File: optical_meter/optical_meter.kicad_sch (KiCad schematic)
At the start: 43 parts, among them J1 SFP+, J2 SFP+, J3 Conn_01x02_Pin, U2 FIN1002M5X, U3 FIN1001M5X

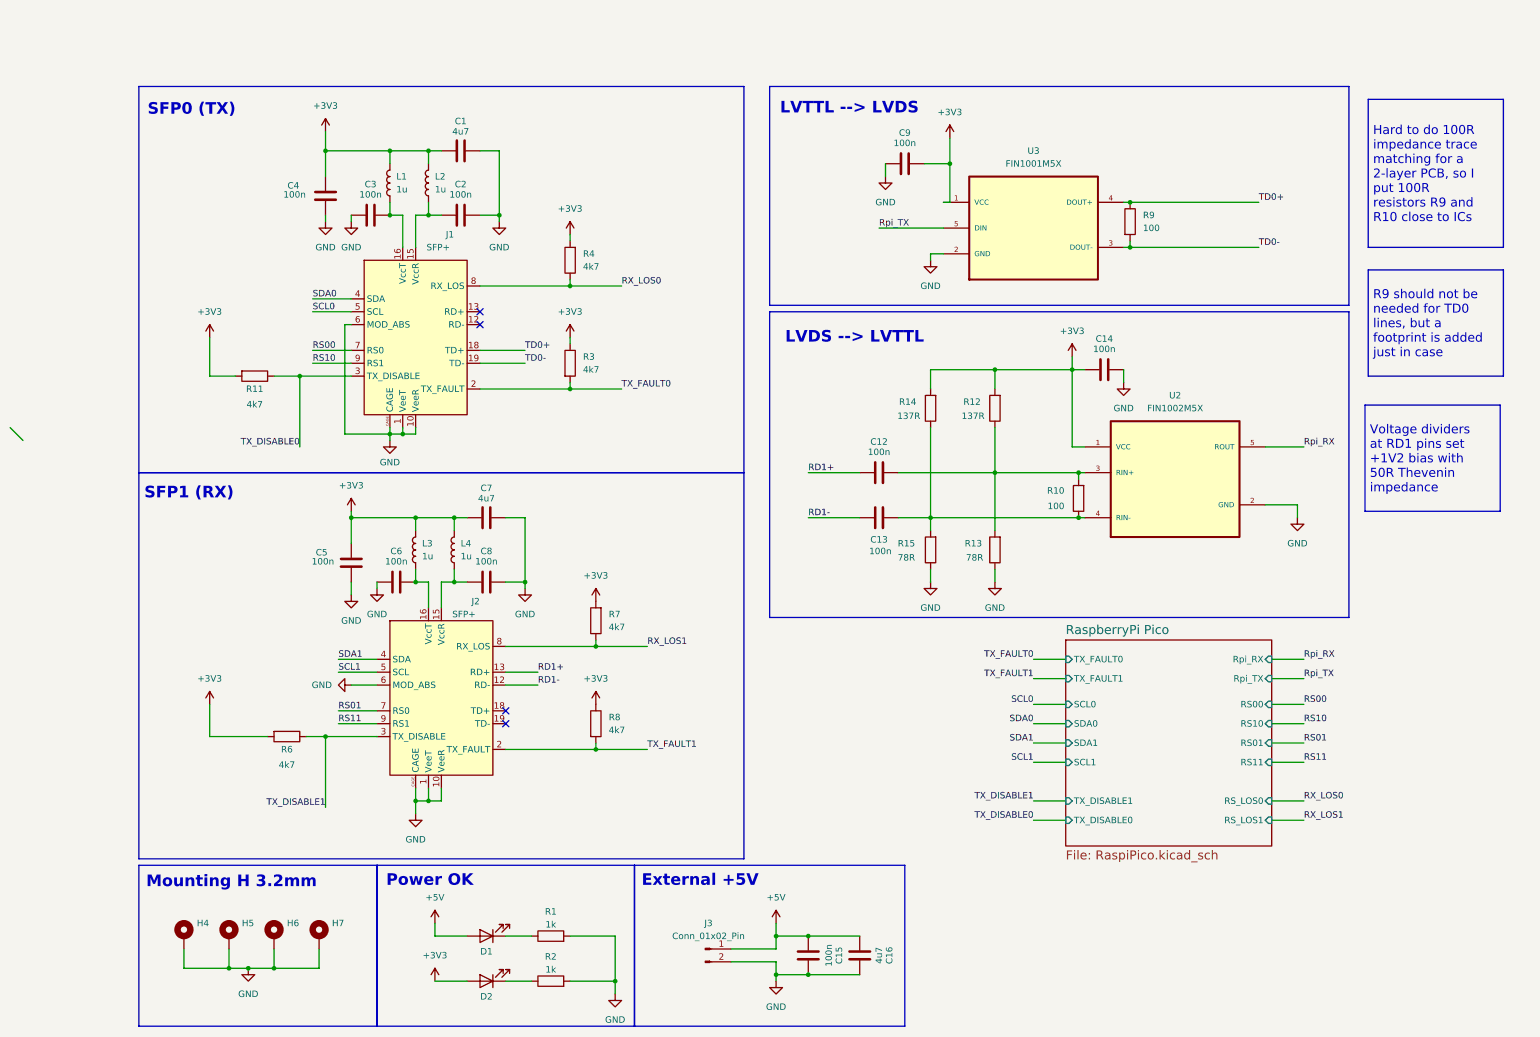
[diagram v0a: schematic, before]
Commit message: Removing one SFP connector - now the PCB will only work with full-duplex SFP/SFT+ connectors. Also did a major schematic cleanup: no hierarchal design, added 2 more GPIOs, DNP voltage dividers on LVDS lines creating +1V2 offset
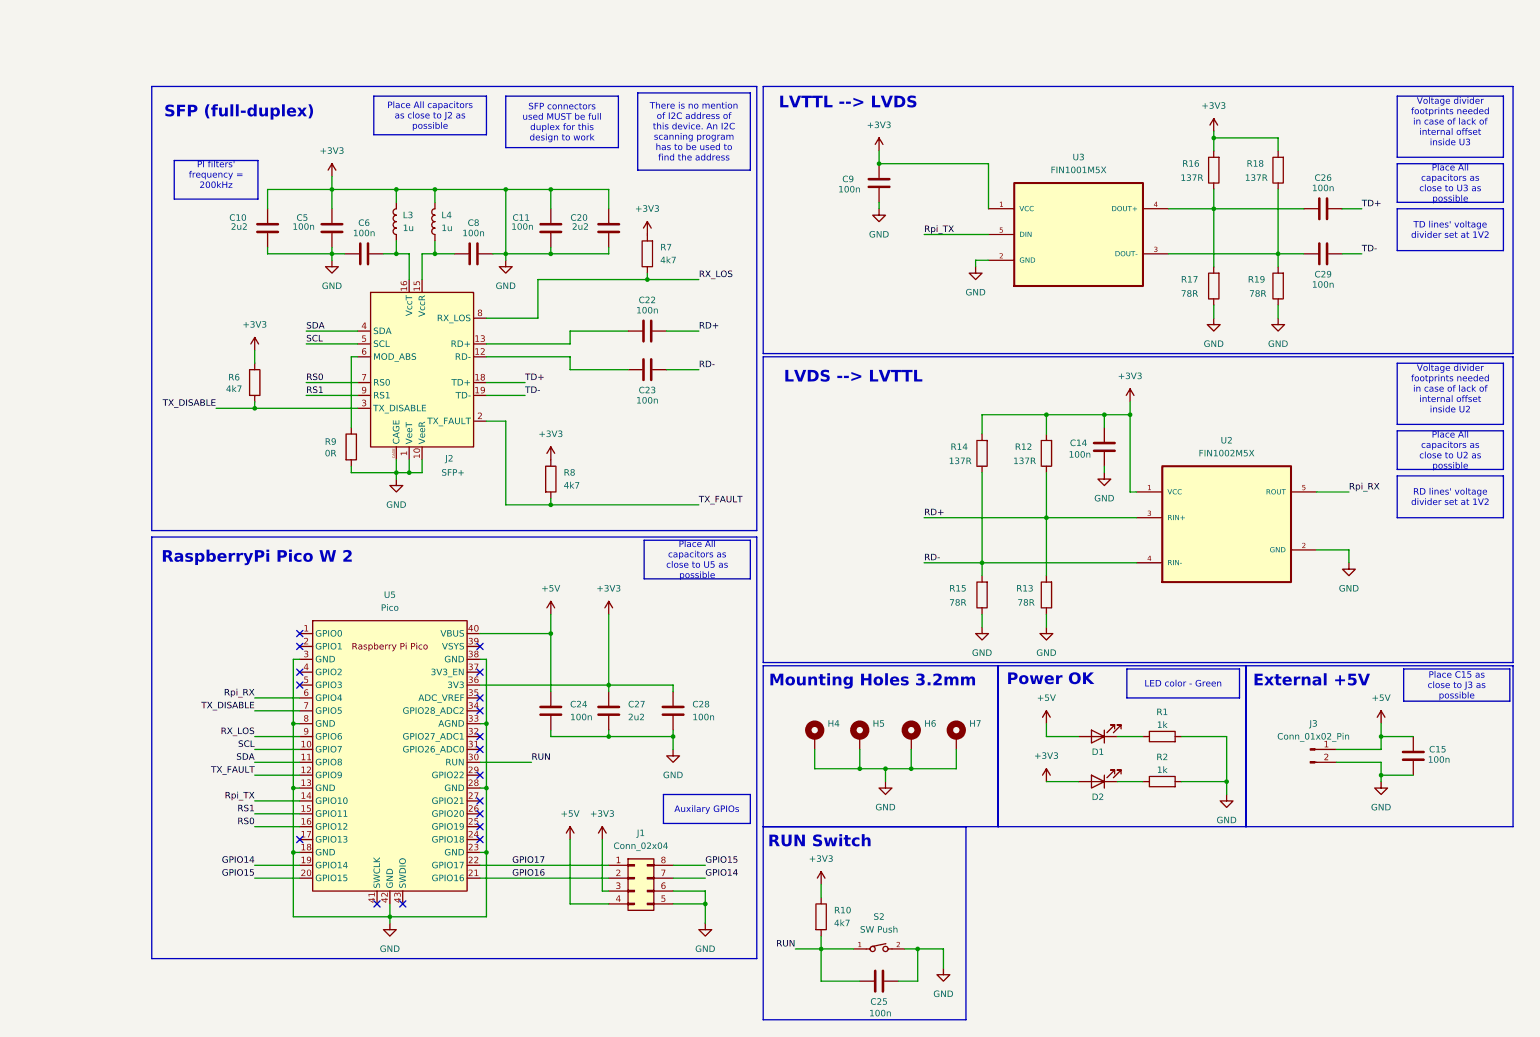
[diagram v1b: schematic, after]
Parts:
- removed C1, C16, C7: 4u7, Capacitor_SMD:C_0603_1608Metric, symbol Device:C
- removed C12, C13, C2, C3, C4: 100n, Capacitor_SMD:C_0603_1608Metric, symbol Device:C
- removed J1: SFP+, SFP:Connector_SFP_and_Cage, symbol Interface_Optical:SFP+
- removed L1, L2: 1u, Inductor_SMD:L_0805_2012Metric_Pad1.15x1.40mm_HandSolder, symbol Device:L
- removed R11, R3, R4: 4k7, Resistor_SMD:R_0603_1608Metric_Pad0.98x0.95mm_HandSolder, symbol Device:R
- added C10, C20, C27: 2u2, Capacitor_SMD:C_0603_1608Metric, symbol Device:C
- added C11, C22, C23, C24, C25, C26, C28, C29: 100n, Capacitor_SMD:C_0603_1608Metric, symbol Device:C
- added J1: Conn_02x04, symbol Connector_Generic:Conn_02x04_Counter_Clockwise
- added R16, R18: 137R, Resistor_SMD:R_0603_1608Metric_Pad0.98x0.95mm_HandSolder, symbol Device:R
- added R17, R19: 78R, Resistor_SMD:R_0603_1608Metric_Pad0.98x0.95mm_HandSolder, symbol Device:R
- added S2: SW Push, SW_Push:434123025816, symbol SW_Push:434123025816
- added U5: Pico, MCU_RaspberryPi_and_Boards:RPi_Pico_SMD_TH, symbol MCU_RaspberryPi_and_Boards:Pico
- R10: value 100 -> 4k7
- R9: value 100 -> 0R
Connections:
- net +3V3: now also C14.1, C15.2, C5.1, C6.1, C8.2, C9.1, H4.1, H5.1, H6.1, H7.1, J2.1 (VeeT), J2.10 (VeeR), J2.11 (VeeR), J2.14 (VeeR), J2.17 (VeeT), J2.20 (VeeT), J2.CAGE, J3.2 (Pin_2), R1.2, R10.1, R13.1, R15.1, R2.2, R6.1, R9.2, U2.2 (GND), U3.2 (GND), C10.1, C10.2, C11.1, C11.2, C20.1, C20.2, C24.2, C25.1, C27.1, C27.2, C28.1, C28.2, J1.3 (Pin_3), J1.5 (Pin_5), J1.6 (Pin_6), R16.2, R17.1, R18.2, R19.1, S2.2, U5.13 (GND), U5.18 (GND), U5.23 (GND), U5.28 (GND), U5.3 (GND), U5.33 (AGND), U5.36 (3V3), U5.38 (GND), U5.42 (GND), U5.8 (GND); no longer R6.2
- net +5V: now also C24.1, J1.4 (Pin_4), U5.40 (VBUS)
- net Rpi_RX: now also U5.6 (GPIO4)
- net Rpi_TX: now also U5.14 (GPIO10)
- net RD-: now reaches R14.1, R15.2, U2.4 (RIN-)
- net RD-: now also C23.2; no longer R10.1
- net RD+: now reaches R12.1, R13.2, U2.3 (RIN+)
- net RD+: now also C22.2; no longer R10.2
- net TD+: now reaches J2.18 (TD+)
- net TD+: now also C26.2
- net TD-: now reaches J2.19 (TD-)
- net TD-: now also C29.2
- removed net GND: C14.1, C15.2, C5.1, C6.1, C8.2, C9.1, H4.1, H5.1, H6.1, H7.1, J2.1 (VeeT), J2.10 (VeeR), J2.11 (VeeR), J2.14 (VeeR), J2.17 (VeeT), J2.20 (VeeT), J2.6 (MOD_ABS), J2.CAGE, J3.2 (Pin_2), R1.2, R13.1, R15.1, R2.2, U2.2 (GND), U3.2 (GND)
- net RD1+: no longer names the net of J2.13 (RD+)
- net RD1+: now also C22.1
- net RD1-: no longer names the net of J2.12 (RD-)
- net RD1-: now also C23.1
- net RS01 renamed RS0
- net RS0: now also U5.16 (GPIO12)
- net RS11 renamed RS1
- net RS1: now also U5.15 (GPIO11)
- net RX_LOS1 renamed RX_LOS
- net RX_LOS: now also U5.9 (GPIO6)
- net SCL1 renamed SCL
- net SCL: now also U5.10 (GPIO7)
- net SDA1 renamed SDA
- net SDA: now also U5.11 (GPIO8)
- net TD0+: no longer names the net of U3.4 (DOUT+)
- net TD0+: now also C26.1, R16.1, R17.2; no longer R9.1
- net TD0-: no longer names the net of U3.3 (DOUT-)
- net TD0-: now also C29.1, R18.1, R19.2; no longer R9.2
- net TX_DISABLE1 renamed TX_DISABLE
- net TX_DISABLE: now also R6.2, U5.7 (GPIO5); no longer R6.1
- net TX_FAULT1 renamed TX_FAULT
- net TX_FAULT: now also U5.12 (GPIO9)
- new net: J2.6 (MOD_ABS), R9.1
- new net GPIO14: J1.7 (Pin_7), U5.19 (GPIO14)
- new net GPIO15: J1.8 (Pin_8), U5.20 (GPIO15)
- new net GPIO16: J1.2 (Pin_2), U5.21 (GPIO16)
- new net GPIO17: J1.1 (Pin_1), U5.22 (GPIO17)
- new net RUN: C25.2, R10.2, S2.1, U5.30 (RUN)
- no-connect marks 4 -> 18
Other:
- removed sheet RaspberryPi Pico
- note added: "Mounting Holes 3.2mm"
- note added: "RUN Switch"
- note added: "RaspberryPi Pico W 2"
- note added: "SFP (full-duplex)"
- note removed: "Mounting H 3.2mm"
- note removed: "SFP0 (TX)"
- note removed: "SFP1 (RX)"
- moved on the sheet: C14, C15, C5, C6, C8, C9, D1, D2, H4, H5, H6, H7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

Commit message: Fixing some 3D model file paths
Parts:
- J1: footprint (none) -> Connector_PinHeader_2.54mm:PinHeader_2x04_P2.54mm_Vertical
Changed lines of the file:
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@@
 		(dnp no)
 		(property "Reference" "J2"
-			(at 73.152 86.106 0)
+			(at 71.882 48.768 0)
 			(effects
 				(font
@@
 		)
 		(property "Value" "SFP+"
-			(at 72.39 88.9 0)
+			(at 71.12 51.562 0)
 			(effects
 				(font
@@
 			)
 		)
-		(property "Footprint" ""
+		(property "Footprint" "Connector_PinHeader_2.54mm:PinHeader_2x04_P2.54mm_Vertical"
 			(at 110.49 168.91 0)
 			(effects

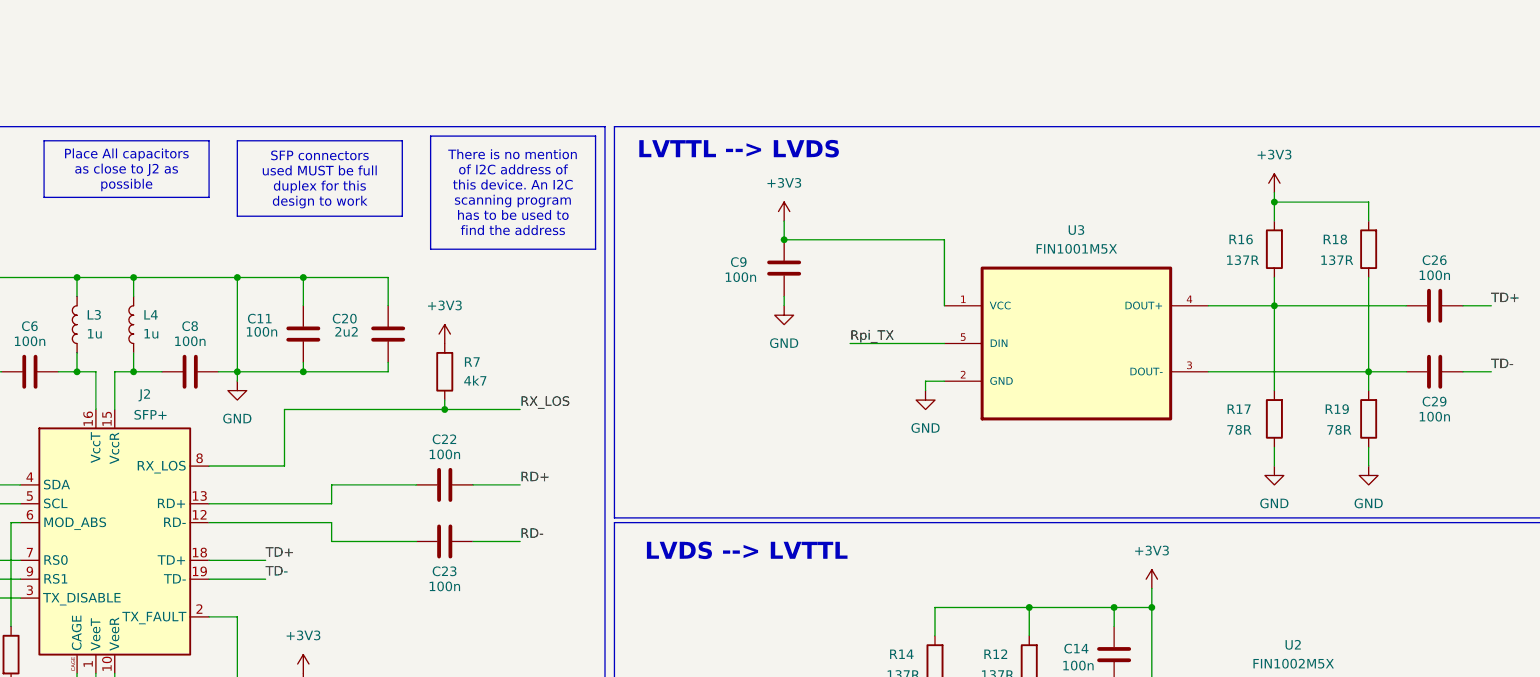
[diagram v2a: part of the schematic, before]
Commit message: fixing accidental short of GND to 3v3
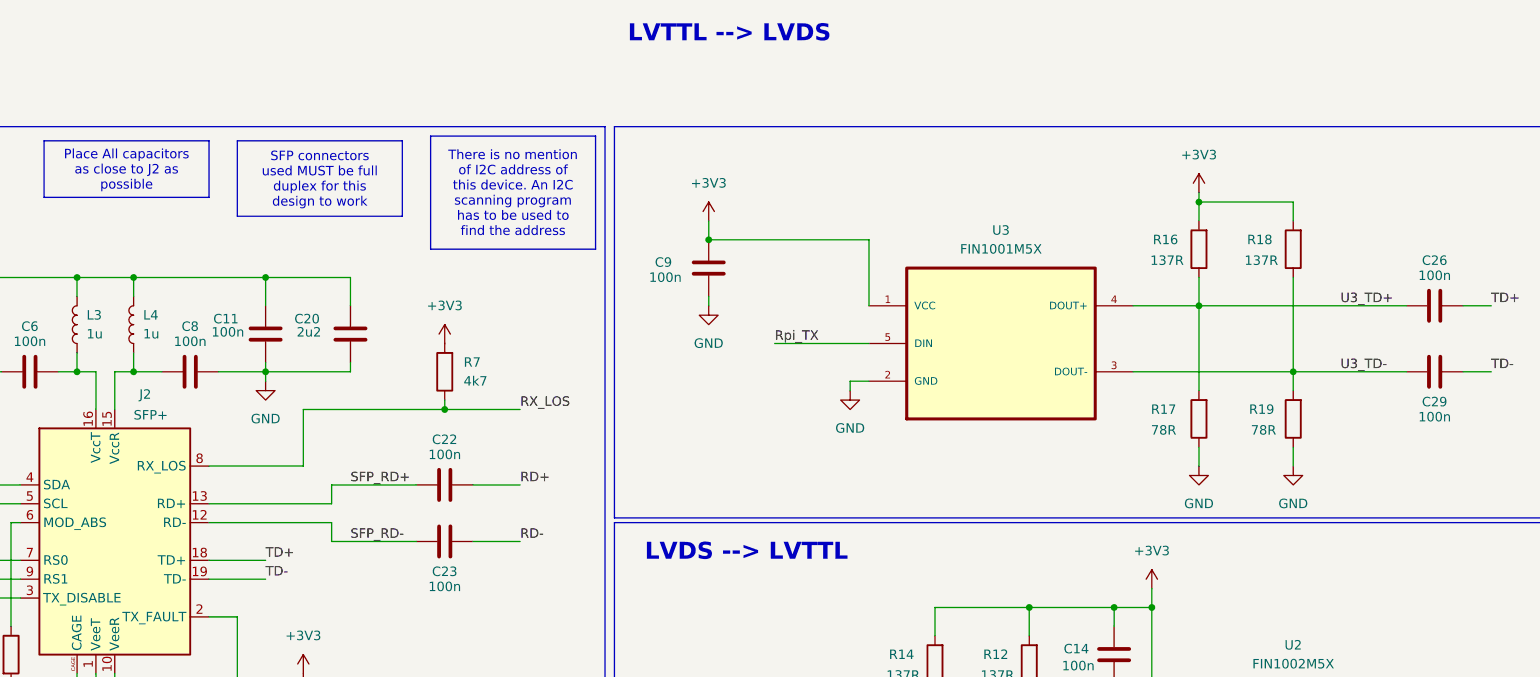
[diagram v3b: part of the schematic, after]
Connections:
- net +3V3: no longer C10.1, C11.1, C14.2, C15.2, C20.1, C24.2, C25.1, C27.2, C28.2, C5.1, C6.1, C8.2, C9.1, H4.1, H5.1, H6.1, H7.1, J1.5 (Pin_5), J1.6 (Pin_6), J2.1 (VeeT), J2.10 (VeeR), J2.11 (VeeR), J2.14 (VeeR), J2.17 (VeeT), J2.20 (VeeT), J2.CAGE, J3.2 (Pin_2), R1.2, R13.1, R15.1, R17.1, R19.1, R2.2, R9.2, S2.2, U2.2 (GND), U3.2 (GND), U5.13 (GND), U5.18 (GND), U5.23 (GND), U5.28 (GND), U5.3 (GND), U5.33 (AGND), U5.38 (GND), U5.42 (GND), U5.8 (GND)
- net U3_TD+: now reaches C26.1, R16.1, R17.2, U3.4 (DOUT+)
- net U3_TD-: now reaches C29.1, R18.1, R19.2, U3.3 (DOUT-)
- net SFP_RD-: now reaches C23.1, J2.12 (RD-)
- net SFP_RD+: now reaches C22.1, J2.13 (RD+)
- new net GND: C10.1, C11.1, C14.2, C15.2, C20.1, C24.2, C25.1, C27.2, C28.2, C5.1, C6.1, C8.2, C9.1, H4.1, H5.1, H6.1, H7.1, J1.5 (Pin_5), J1.6 (Pin_6), J2.1 (VeeT), J2.10 (VeeR), J2.11 (VeeR), J2.14 (VeeR), J2.17 (VeeT), J2.20 (VeeT), J2.CAGE, J3.2 (Pin_2), R1.2, R13.1, R15.1, R17.1, R19.1, R2.2, R9.2, S2.2, U2.2 (GND), U3.2 (GND), U5.13 (GND), U5.18 (GND), U5.23 (GND), U5.28 (GND), U5.3 (GND), U5.33 (AGND), U5.38 (GND), U5.42 (GND), U5.8 (GND)
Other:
- moved on the sheet: C11, C20, C9, R16, R17, R18, R19, U3
